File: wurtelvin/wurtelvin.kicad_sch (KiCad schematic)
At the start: 33 parts, among them J1 BATT, J2 FRONT, J3 MIRRORS, J4 REAR TURNERS, J5 REAR, J6 BTN_BRK, J7 btn_handle, SW1 ON/OFF, SW2 DAYLIGHT, SW3 DIM, SW4 REAR, U1 STM32F103C8Tx, Y1 8MHz

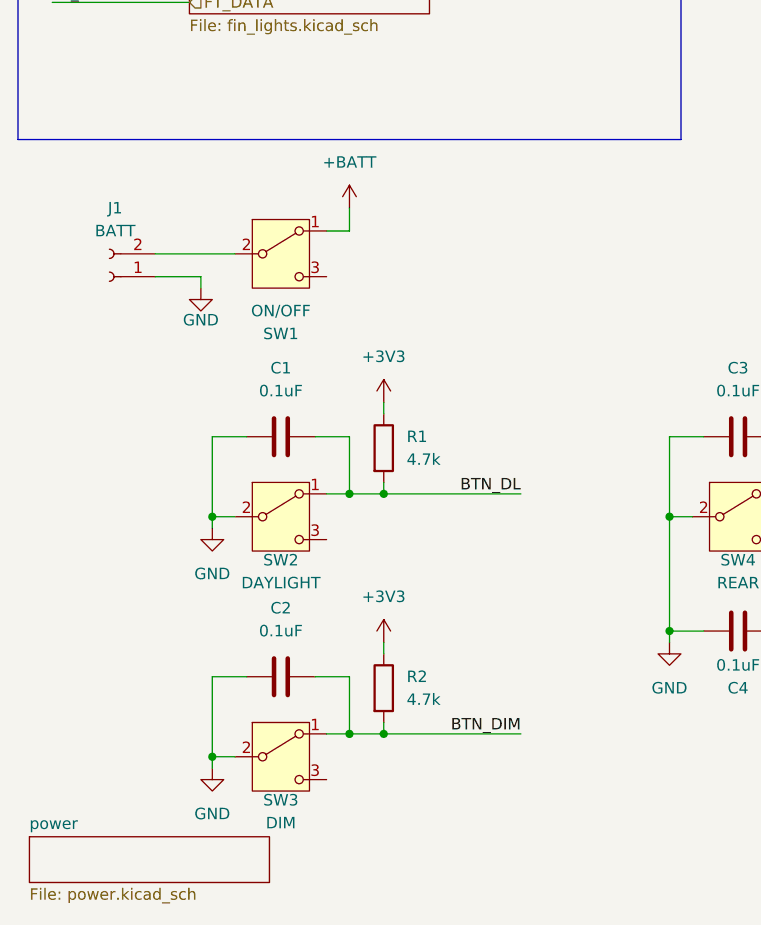
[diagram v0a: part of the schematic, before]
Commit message: started pcb layout for connector and 3v3 and 5v step-down
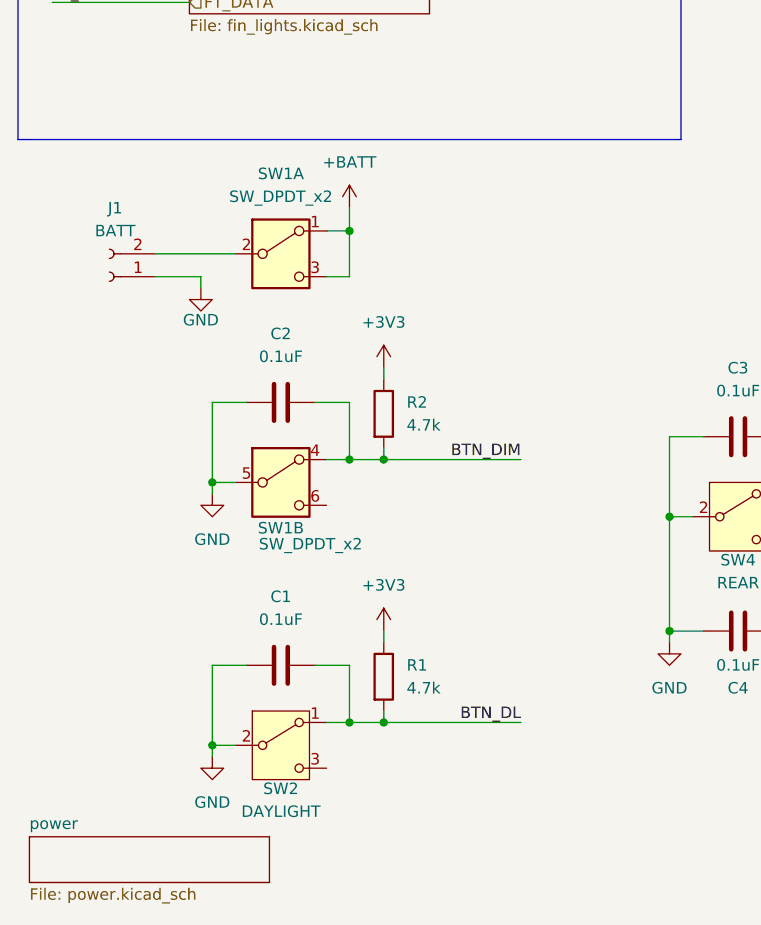
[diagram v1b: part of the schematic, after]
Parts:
- removed SW1: ON/OFF, Library:KNX1, symbol Switch:SW_SPDT
- removed SW3: DIM, Library:KNX1, symbol Switch:SW_SPDT
- added SW1: SW_DPDT_x2, Library:ANT_2x3, symbol Switch:SW_DPDT_x2
- SW2, SW4: footprint Library:KNX1 -> Library:ANT_1x3
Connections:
- net +BATT: now also SW1.1 (A), SW1.3 (C)
- net BTN_DIM: now also SW1.4 (A)
- net GND: now also SW1.5 (B)
- net at J1.2 (Pin_2): now also SW1.2 (B)
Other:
- moved on the sheet: C1, C2, R1, R2, SW2

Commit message: furhter pcb layout
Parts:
- renumbered C5 to C1, C4 to C10, C1 to C11, C6 to C2, C7 to C3, C8 to C4, C9 to C5, C2 to C6, C10 to C7, C3 to C8, C11 to C9, J2 to J1, J3 to J2, J4 to J3, J5 to J4, J6 to J5, J1 to J6, R5 to R1, R7 to R2, R8 to R3, R2 to R4, R6 to R5, R3 to R6, R4 to R7, R1 to R8, SW4 to SW2, SW2 to SW3
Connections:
- net OSC32_IN: no longer names the net of U1.3 (PC14)
- net OSC32_OUT: no longer names the net of U1.4 (PC15)
- no-connect marks 0 -> 37
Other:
- sheet fin_lights ports: added FF_DATA, FR_DATA, FT_DATA; removed none
- sheet front_lights ports: added CTRL_DL, CTRL_FH, CTRL_FL, DL+, DL-, FH+, FH-, FL+, FL-; removed none
- sheet rear_lights ports: added BRK+, BRK-, CTRL_BRK, CTRL_REAR, REAR+, REAR-; removed none
- sheet turning_lights ports: added CTRL_TLL, CTRL_TLR, TLL+, TLL-, TLR+, TLR-; removed none
